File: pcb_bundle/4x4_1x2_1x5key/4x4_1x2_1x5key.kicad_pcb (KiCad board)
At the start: 2 copper layers, 100.8 x 91.5 mm, 103 parts

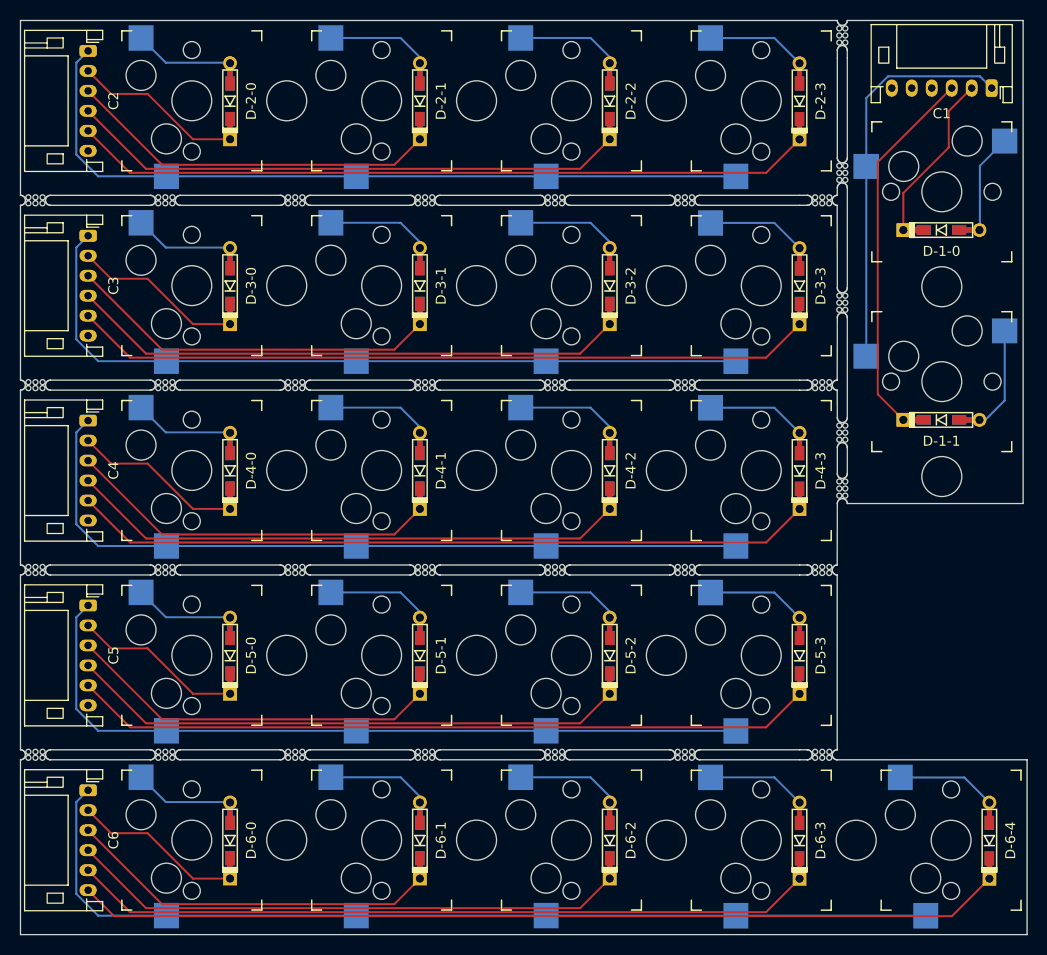
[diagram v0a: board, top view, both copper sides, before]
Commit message: v0.1b: manufacturer friendly mousebite
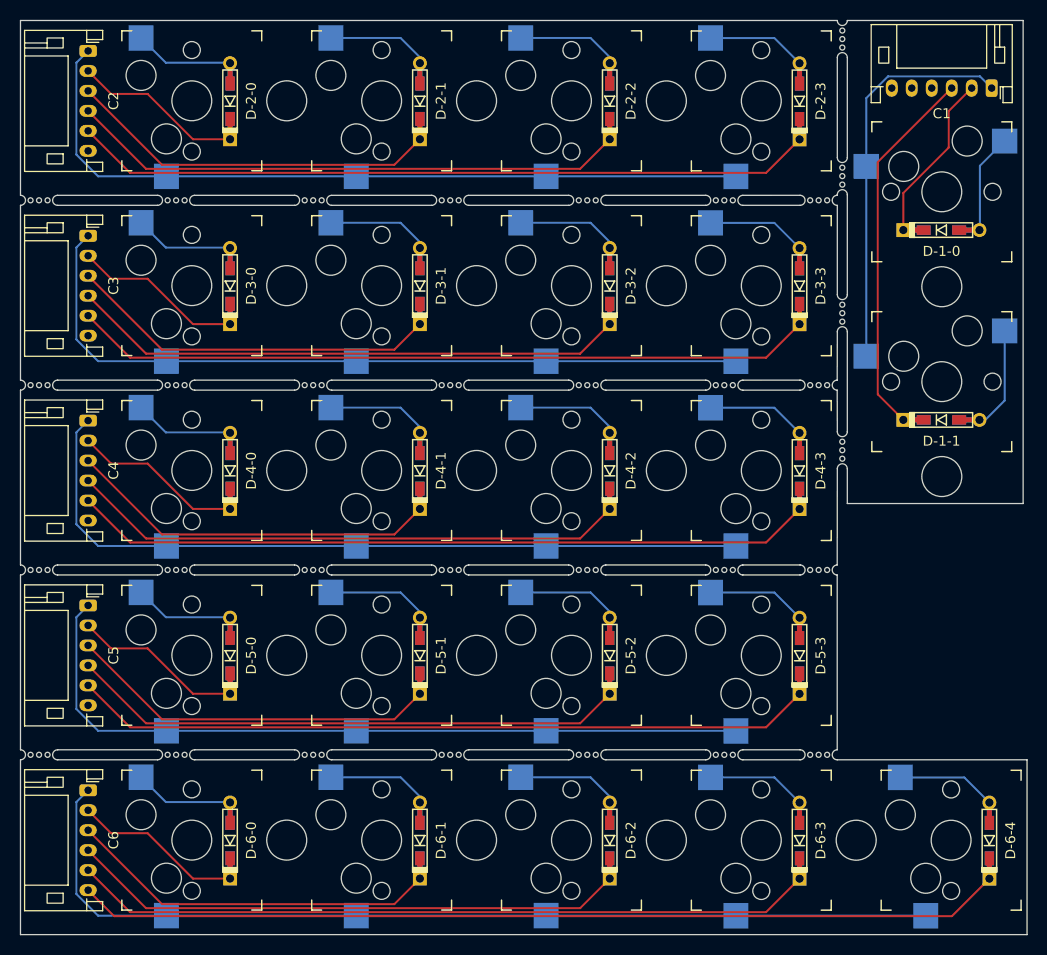
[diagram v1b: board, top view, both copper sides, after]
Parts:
- removed the mouse-bite-1mm-3mm at (77.3, 146.0)
- removed the mouse-bite-1mm-3mm at (64.3, 109.0)
- removed the mouse-bite-1mm-3mm at (51.3, 90.5)
- removed the mouse-bite-1mm-3mm at (77.3, 127.5)
- removed the mouse-bite-1mm-3mm at (104.0, 109.0)
- removed the mouse-bite-1mm-3mm at (90.3, 90.5)
- removed the mouse-bite-1mm-3mm at (51.3, 127.5)
- removed the mouse-bite-1mm-3mm at (106.0, 87.8)
- removed the mouse-bite-1mm-3mm at (38.3, 146.0)
- removed the mouse-bite-1mm-3mm at (90.3, 146.0)
- removed the mouse-bite-1mm-3mm at (64.3, 90.5)
- removed the mouse-bite-1mm-3mm at (104.0, 146.0)
- removed the mouse-bite-1mm-3mm at (38.3, 127.5)
- removed the mouse-bite-1mm-3mm at (104.0, 90.6)
- removed the mouse-bite-1mm-3mm at (104.0, 127.5)
- removed the mouse-bite-1mm-3mm at (25.3, 127.5)
- removed the mouse-bite-1mm-3mm at (106.0, 100.8)
- removed the mouse-bite-1mm-3mm at (106.0, 74.0)
- removed the mouse-bite-1mm-3mm at (38.3, 90.5)
- removed the mouse-bite-1mm-3mm at (25.3, 90.5)
- removed the mouse-bite-1mm-3mm at (38.3, 109.0)
- removed the mouse-bite-1mm-3mm at (106.0, 113.8)
- removed the mouse-bite-1mm-3mm at (64.3, 146.0)
- removed the mouse-bite-1mm-3mm at (64.3, 127.5)
- removed the mouse-bite-1mm-3mm at (51.3, 109.0)
- removed the mouse-bite-1mm-3mm at (25.3, 146.0)
- removed the mouse-bite-1mm-3mm at (90.3, 109.0)
- removed the mouse-bite-1mm-3mm at (106.0, 119.4)
- removed the mouse-bite-1mm-3mm at (77.3, 109.0)
- removed the mouse-bite-1mm-3mm at (90.3, 127.5)
- removed the mouse-bite-1mm-3mm at (51.3, 146.0)
- removed the mouse-bite-1mm-3mm at (77.3, 90.5)
- removed the mouse-bite-1mm-3mm at (25.3, 109.0)
- added mouse-bite-1mm-3mm: VAL**, Panelization:BreakLine_3h_D0.5mm_P0.85mm, F.Cu at (39.4, 109.1)
- added mouse-bite-1mm-3mm: VAL**, Panelization:BreakLine_3h_D0.5mm_P0.85mm, F.Cu at (80.5, 127.6)
- added mouse-bite-1mm-3mm: VAL**, Panelization:BreakLine_3h_D0.5mm_P0.85mm, F.Cu at (25.6, 109.1)
- added mouse-bite-1mm-3mm: VAL**, Panelization:BreakLine_3h_D0.5mm_P0.85mm, F.Cu at (66.8, 109.1)
- added mouse-bite-1mm-3mm: VAL**, Panelization:BreakLine_3h_D0.5mm_P0.85mm, F.Cu at (53.1, 109.1)
- added mouse-bite-1mm-3mm: VAL**, Panelization:BreakLine_3h_D0.5mm_P0.85mm, F.Cu at (94.2, 90.6)
- added mouse-bite-1mm-3mm: VAL**, Panelization:BreakLine_3h_D0.5mm_P0.85mm, F.Cu at (106.0, 101.8)
- added mouse-bite-1mm-3mm: VAL**, Panelization:BreakLine_3h_D0.5mm_P0.85mm, F.Cu at (103.7, 127.5)
- added mouse-bite-1mm-3mm: VAL**, Panelization:BreakLine_3h_D0.5mm_P0.85mm, F.Cu at (39.4, 90.6)
- added mouse-bite-1mm-3mm: VAL**, Panelization:BreakLine_3h_D0.5mm_P0.85mm, F.Cu at (53.1, 127.6)
- added mouse-bite-1mm-3mm: VAL**, Panelization:BreakLine_3h_D0.5mm_P0.85mm, F.Cu at (103.7, 90.6)
- added mouse-bite-1mm-3mm: VAL**, Panelization:BreakLine_3h_D0.5mm_P0.85mm, F.Cu at (25.6, 127.6)
- added mouse-bite-1mm-3mm: VAL**, Panelization:BreakLine_3h_D0.5mm_P0.85mm, F.Cu at (80.5, 90.6)
- added mouse-bite-1mm-3mm: VAL**, Panelization:BreakLine_3h_D0.5mm_P0.85mm, F.Cu at (80.5, 146.1)
- added mouse-bite-1mm-3mm: VAL**, Panelization:BreakLine_3h_D0.5mm_P0.85mm, F.Cu at (66.8, 90.6)
- added mouse-bite-1mm-3mm: VAL**, Panelization:BreakLine_3h_D0.5mm_P0.85mm, F.Cu at (106.0, 115.6)
- added mouse-bite-1mm-3mm: VAL**, Panelization:BreakLine_3h_D0.5mm_P0.85mm, F.Cu at (103.7, 146.0)
- added mouse-bite-1mm-3mm: VAL**, Panelization:BreakLine_3h_D0.5mm_P0.85mm, F.Cu at (106.0, 88.1)
- added mouse-bite-1mm-3mm: VAL**, Panelization:BreakLine_3h_D0.5mm_P0.85mm, F.Cu at (80.5, 109.1)
- added mouse-bite-1mm-3mm: VAL**, Panelization:BreakLine_3h_D0.5mm_P0.85mm, F.Cu at (53.1, 90.6)
- added mouse-bite-1mm-3mm: VAL**, Panelization:BreakLine_3h_D0.5mm_P0.85mm, F.Cu at (39.4, 146.1)
- added mouse-bite-1mm-3mm: VAL**, Panelization:BreakLine_3h_D0.5mm_P0.85mm, F.Cu at (25.6, 90.6)
- added mouse-bite-1mm-3mm: VAL**, Panelization:BreakLine_3h_D0.5mm_P0.85mm, F.Cu at (103.7, 109.0)
- added mouse-bite-1mm-3mm: VAL**, Panelization:BreakLine_3h_D0.5mm_P0.85mm, F.Cu at (66.8, 146.1)
- added mouse-bite-1mm-3mm: VAL**, Panelization:BreakLine_3h_D0.5mm_P0.85mm, F.Cu at (53.1, 146.1)
- added mouse-bite-1mm-3mm: VAL**, Panelization:BreakLine_3h_D0.5mm_P0.85mm, F.Cu at (94.2, 109.1)
- added mouse-bite-1mm-3mm: VAL**, Panelization:BreakLine_3h_D0.5mm_P0.85mm, F.Cu at (25.6, 146.1)
- added mouse-bite-1mm-3mm: VAL**, Panelization:BreakLine_3h_D0.5mm_P0.85mm, F.Cu at (106.0, 74.4)
- added mouse-bite-1mm-3mm: VAL**, Panelization:BreakLine_3h_D0.5mm_P0.85mm, F.Cu at (39.4, 127.6)
- added mouse-bite-1mm-3mm: VAL**, Panelization:BreakLine_3h_D0.5mm_P0.85mm, F.Cu at (66.8, 127.6)
- added mouse-bite-1mm-3mm: VAL**, Panelization:BreakLine_3h_D0.5mm_P0.85mm, F.Cu at (94.2, 146.1)
- added mouse-bite-1mm-3mm: VAL**, Panelization:BreakLine_3h_D0.5mm_P0.85mm, F.Cu at (94.2, 127.6)
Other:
- outline, holes or cut-outs redrawn
